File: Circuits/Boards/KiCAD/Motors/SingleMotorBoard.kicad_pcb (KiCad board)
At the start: 2 copper layers, 63.5 x 84.8 mm, 45 parts, among them M1 IRFS7537PBF, M2 IRFS7537PBF, M3 IRFS7537PBF, M4 IRFS7537PBF, Q1 2N3904, Q2 2N3904, Q3 2N3904, Q4 2N3904, Q5 2N3904, Q6 2N3904, Q7 2N3904, Q8 2N3904

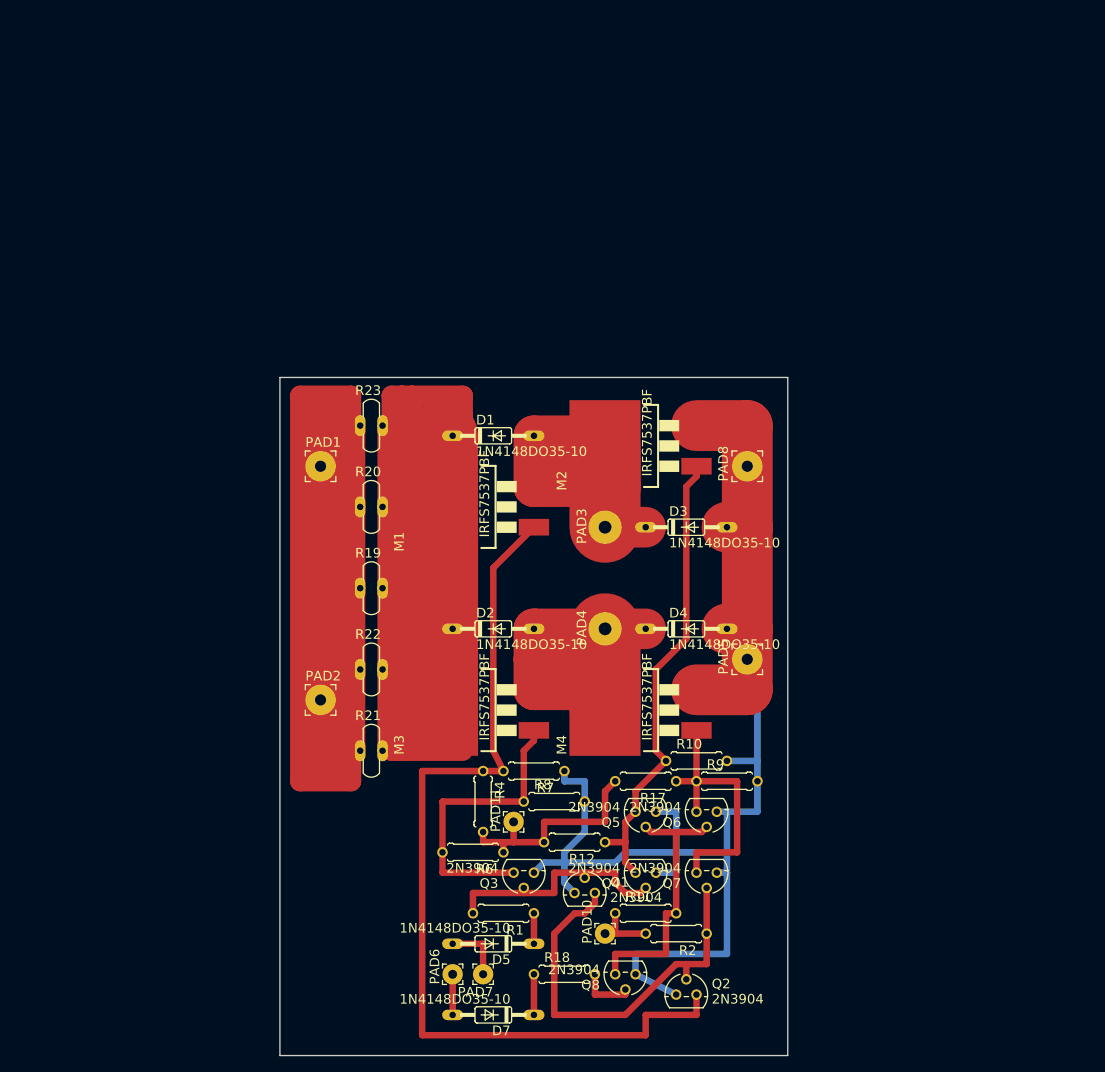
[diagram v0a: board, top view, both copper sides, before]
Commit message: Update KiCAD motor controller and Version 2 simulation
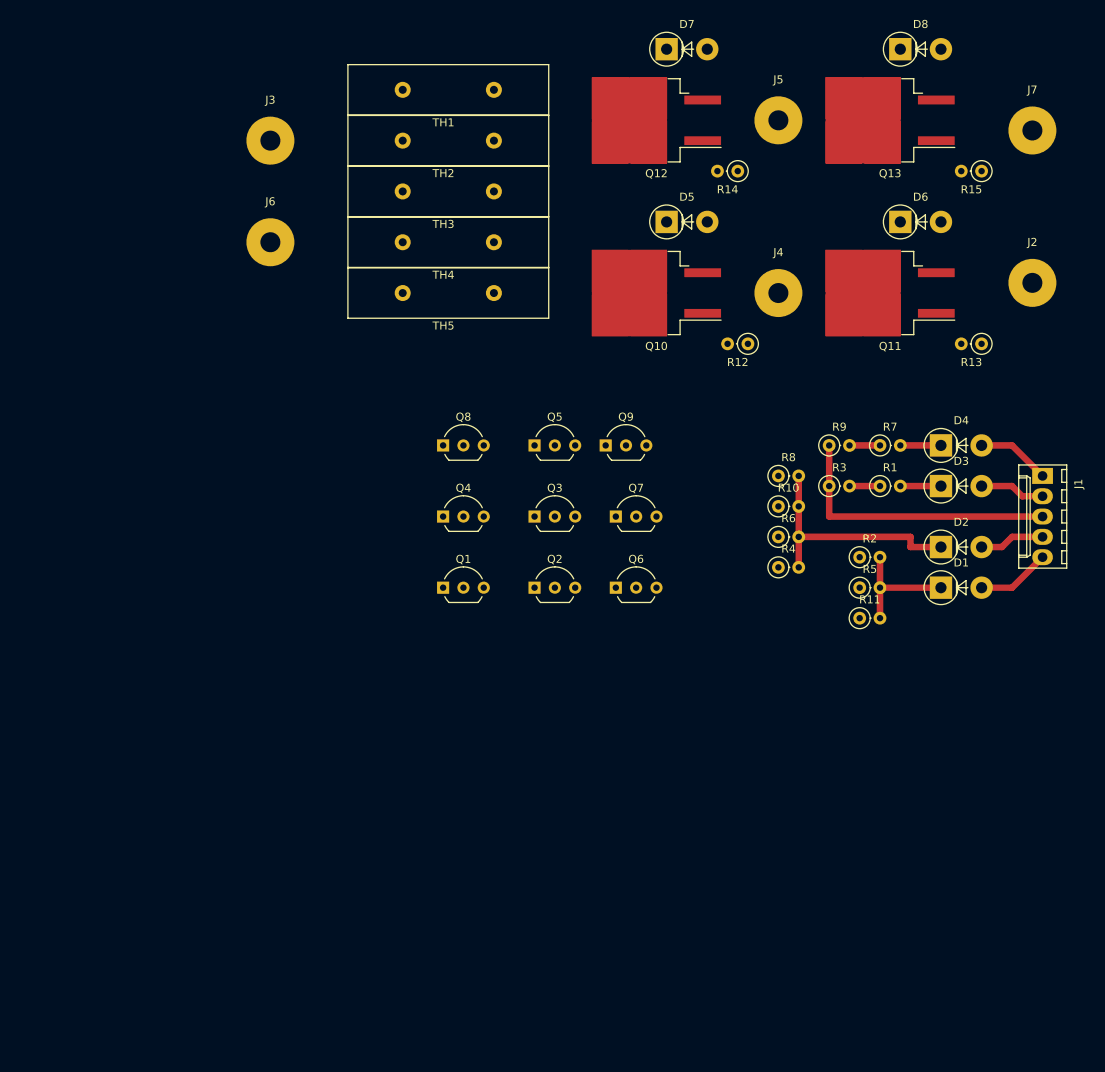
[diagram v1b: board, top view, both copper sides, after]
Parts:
- removed M1, M2, M3, M4: IRFS7537PBF, D2PACK
- removed PAD1, PAD2, PAD5, PAD8: , 3,81%2f1,4
- removed PAD10, PAD11, PAD6: , 2,54%2f1,1
- removed PAD3, PAD4: WIREPAD4,16O1,6, 4,16O1,6
- removed PAD7: , 2,54%2f1,0
- removed R17, R18: , 0207%2f7
- removed R19, R20, R21, R22, R23: , P660A
- added D6: 1N4007, Diodes_THT:D_5W_P5.08mm_Vertical_AnodeUp, F.Cu at (194.3, 43.2)
- added D8: 1N4007, Diodes_THT:D_5W_P5.08mm_Vertical_AnodeUp, F.Cu at (194.3, 21.6)
- added J1: Conn_01x05, Connectors_Molex:Molex_KK-6410-05_05x2.54mm_Straight, F.Cu at (212.1, 74.9)
- added J2: Conn_01x01, Wire_Pads:SolderWirePad_single_2-5mmDrill, F.Cu at (210.8, 50.8)
- added J3: Conn_01x01, Wire_Pads:SolderWirePad_single_2-5mmDrill, F.Cu at (115.6, 33.0)
- added J4: Conn_01x01, Wire_Pads:SolderWirePad_single_2-5mmDrill, F.Cu at (179.1, 52.1)
- added J5: Conn_01x01, Wire_Pads:SolderWirePad_single_2-5mmDrill, F.Cu at (179.1, 30.5)
- added J6: Conn_01x01, Wire_Pads:SolderWirePad_single_2-5mmDrill, F.Cu at (115.6, 45.7)
- added J7: Conn_01x01, Wire_Pads:SolderWirePad_single_2-5mmDrill, F.Cu at (210.8, 31.8)
- added Q10: Q_NMOS_DGS, TO_SOT_Packages_SMD:TO-263-2, F.Cu at (163.8, 52.1)
- added Q11: Q_NMOS_DGS, TO_SOT_Packages_SMD:TO-263-2, F.Cu at (193.0, 52.1)
- added Q12: Q_NMOS_DGS, TO_SOT_Packages_SMD:TO-263-2, F.Cu at (163.8, 30.5)
- added Q13: Q_NMOS_DGS, TO_SOT_Packages_SMD:TO-263-2, F.Cu at (193.0, 30.5)
- added Q9: 2N3904, TO_SOT_Packages_THT:TO-92_Inline_Wide, F.Cu at (157.5, 71.1)
- added R13: 10K, Resistors_THT:R_Axial_DIN0207_L6.3mm_D2.5mm_P2.54mm_Vertical, F.Cu at (204.5, 58.4)
- added R14: 1Meg, Resistors_THT:R_Axial_DIN0207_L6.3mm_D2.5mm_P2.54mm_Vertical, F.Cu at (174.0, 36.8)
- added R15: 10K, Resistors_THT:R_Axial_DIN0207_L6.3mm_D2.5mm_P2.54mm_Vertical, F.Cu at (204.5, 36.8)
- added R3: 10K, Resistors_THT:R_Axial_DIN0207_L6.3mm_D2.5mm_P2.54mm_Vertical, F.Cu at (185.4, 76.2)
- added R5: 1K, Resistors_THT:R_Axial_DIN0207_L6.3mm_D2.5mm_P2.54mm_Vertical, F.Cu at (189.2, 88.9)
- added TH1: Thermistor_PTC, Fuse_Holders_and_Fuses:Fuse_Littelfuse-LVR200, F.Cu at (143.5, 26.7)
- added TH2: Thermistor_PTC, Fuse_Holders_and_Fuses:Fuse_Littelfuse-LVR200, F.Cu at (143.5, 33.0)
- added TH3: Thermistor_PTC, Fuse_Holders_and_Fuses:Fuse_Littelfuse-LVR200, F.Cu at (143.5, 39.4)
- added TH4: Thermistor_PTC, Fuse_Holders_and_Fuses:Fuse_Littelfuse-LVR200, F.Cu at (143.5, 45.7)
- added TH5: Thermistor_PTC, Fuse_Holders_and_Fuses:Fuse_Littelfuse-LVR200, F.Cu at (143.5, 52.1)
- D1, D2, D3, D4, D5, D7: value 1N4148DO35-10 -> 1N4007; footprint DO35-10 -> Diodes_THT:D_5W_P5.08mm_Vertical_AnodeUp
- Q1, Q2, Q3, Q4, Q5, Q6, Q7, Q8: footprint TO92 -> TO_SOT_Packages_THT:TO-92_Inline_Wide
- R1, R10, R4, R6, R7, R8, R9: value (none) -> 10K; footprint 0207%2f7 -> Resistors_THT:R_Axial_DIN0207_L6.3mm_D2.5mm_P2.54mm_Vertical
- R11, R2: value (none) -> 1K; footprint 0207%2f7 -> Resistors_THT:R_Axial_DIN0207_L6.3mm_D2.5mm_P2.54mm_Vertical
- R12: value (none) -> 1Meg; footprint 0207%2f7 -> Resistors_THT:R_Axial_DIN0207_L6.3mm_D2.5mm_P2.54mm_Vertical
- moved D7 122.6 mm to (165.1, 21.6), turned to 0 degrees
- moved D5 92.8 mm to (165.1, 43.2), turned to 0 degrees
- moved R1 71.2 mm to (191.8, 76.2), turned to 0 degrees
- moved Q8 69.9 mm to (137.2, 71.1), turned to 0 degrees
- moved R12 66.0 mm to (175.3, 58.4)
- moved R7 59.4 mm to (191.8, 71.1), turned to 0 degrees
- moved D1 59.1 mm to (199.4, 88.9)
- moved D2 56.9 mm to (199.4, 83.8)
- moved R6 54.9 mm to (179.1, 82.5), turned to 0 degrees
- moved Q2 54.3 mm to (148.6, 88.9)
- moved R2 52.3 mm to (189.2, 85.1), turned to 0 degrees
- moved Q4 51.2 mm to (137.2, 80.0), turned to 0 degrees
- moved R8 49.4 mm to (179.1, 74.9)
- moved Q5 47.8 mm to (148.6, 71.1), turned to 0 degrees
- moved R4 47.1 mm to (179.1, 86.4), turned to 0 degrees
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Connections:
- Q1 pad 1: FB -> GND
- Q1 pad 2: BB -> /MBB
- Q1 pad 3: 0 -> /BBM
- Q2 pad 1: FF -> GND
- Q2 pad 2: FB -> /MFB
- Q2 pad 3: 0 -> /MBB
- Q3 pad 1: BF -> GND
- Q3 pad 2: BB -> Net-(Q3-Pad2)
- Q3 pad 3: 0 -> /MFB
- Q4 pad 1: N$20 -> GND
- Q4 pad 2: BB -> /iSpeed
- Q4 pad 3: 0 -> /BBM
- Q5 pad 1: N$20 -> GND
- Q5 pad 2: N$16 -> /MFB
- Q5 pad 3: 0 -> /MFF
- Q6 pad 1: N$27 -> GND
- Q6 pad 2: N$16 -> /MFB
- Q6 pad 3: 0 -> /FBM
- Q7 pad 1: N$27 -> GND
- Q7 pad 2: FB -> /MBB
- Q7 pad 3: 0 -> /MBF
- Q8 pad 1: N$16 -> GND
- Q8 pad 2: N$23 -> Net-(Q8-Pad2)
- Q8 pad 3: 0 -> /iSpeed
- R1 pad 1: N$19 -> Net-(Q3-Pad2)
- R1 pad 2: BB -> /Dir
- R10 pad 1: N$20 -> /MBF
- R10 pad 2: 0 -> /VG
- R11 pad 1: VSW -> /iSpeed
- R11 pad 2: N$16 -> /VSW
- R12 pad 1: N$20 -> GND
- R12 pad 2: VG -> /MFF
- R2 pad 1: FB -> /MBB
- R2 pad 2: VSW -> /VSW
- R4 pad 1: FF -> /BBM
- R4 pad 2: VG -> /VG
- R6 pad 1: VG -> /MFF
- R6 pad 2: BF -> /VG
- R7 pad 1: 0 -> Net-(Q8-Pad2)
- R7 pad 2: FF -> /Speed
- R8 pad 1: BF -> /FBM
- R8 pad 2: 0 -> /VG
- R9 pad 1: N$27 -> GND
- R9 pad 2: 0 -> Net-(Q8-Pad2)
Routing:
- net VDD: track 255.7 -> 0.00 mm
- net VBAT: track 221.8 -> 0.00 mm
- net 0: track 184.8 -> 0.00 mm
- net FF: track 115.4 -> 0.00 mm
- net MP: track 59.3 -> 0.00 mm
- net N$20: track 58.6 -> 0.00 mm
- net MN: track 53.6 -> 0.00 mm
- net FB: track 51.2 -> 0.00 mm
- net BF: track 37.4 -> 0.00 mm
- net GND: track 0.00 -> 35.6 mm
- net N$27: track 34.3 -> 0.00 mm
- net N$16: track 33.5 -> 0.00 mm
- net /VG: track 0.00 -> 30.5 mm
- net BB: track 30.0 -> 0.00 mm
- net VG: track 28.5 -> 0.00 mm
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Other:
- board outline removed
- net class Default: clearance 0.1524 -> 0.254; trace_width 0.25 -> 0.8128; via_dia 0.6 -> 0.889; via_drill 0.4 -> 0.8128
- rule pad_to_mask_clearance: 0.2 -> 0
- rule trace_clearance: 0.1524 -> 0.254
- rule trace_min: 0.1524 -> 0.254
- rule via_min_drill: 0.3 -> 0.8128
- rule via_min_size: 0.4 -> 0.889

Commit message: Fixed KiCAD motor controller
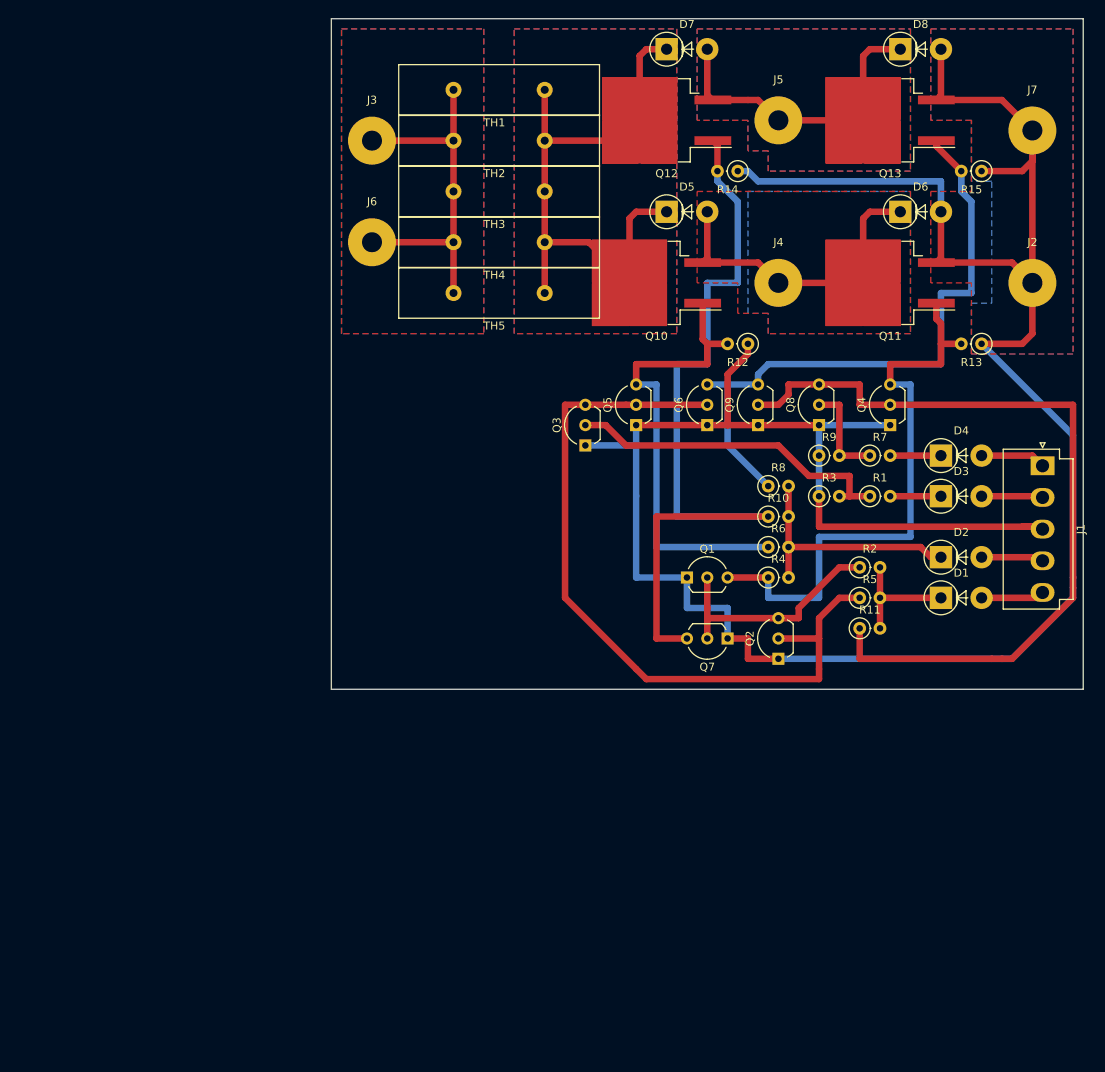
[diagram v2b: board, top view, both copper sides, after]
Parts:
- J1: footprint Connectors_Molex:Molex_KK-6410-05_05x2.54mm_Straight -> Connectors_JST:JST_VH_B5P-VH-B_5x3.96mm_Vertical
- moved Q4 57.0 mm to (193.0, 68.6), turned to 90 degrees
- moved Q8 47.1 mm to (184.2, 68.6), turned to 90 degrees
- moved Q2 31.7 mm to (179.1, 97.8), turned to 90 degrees
- moved Q1 30.5 mm to (167.6, 87.6)
- moved Q6 23.3 mm to (170.2, 68.6), turned to 90 degrees
- moved Q7 20.7 mm to (172.7, 95.2), turned to 180 degrees
- moved Q9 19.2 mm to (176.5, 68.6), turned to 90 degrees
- moved Q5 13.0 mm to (161.3, 68.6), turned to 90 degrees
- moved J3 12.7 mm to (128.3, 33.0)
- moved J6 12.7 mm to (128.3, 45.7)
- moved Q3 10.9 mm to (154.9, 71.1), turned to 90 degrees
- moved TH1 6.35 mm to (149.9, 26.7)
- moved TH2 6.35 mm to (149.9, 33.0)
- moved TH3 6.35 mm to (149.9, 39.4)
- moved TH4 6.35 mm to (149.9, 45.7)
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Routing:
- net GND: track 35.6 -> 330.4 mm
- net /iSpeed: track 0.00 -> 101.5 mm
- net /MBF: track 0.00 -> 100.4 mm
- net /MFB: track 0.00 -> 96.7 mm
- net /FBM: track 0.00 -> 79.4 mm
- net Net-(D5-Pad1): track 0.00 -> 75.8 mm
- net /BBM: track 0.00 -> 73.9 mm
- net /MFF: track 0.00 -> 58.7 mm
- net Net-(J3-Pad1): track 0.00 -> 45.8 mm
- net Net-(D5-Pad2): track 0.00 -> 40.7 mm
- net Net-(D7-Pad2): track 0.00 -> 39.6 mm
- net Net-(Q3-Pad2): track 3.81 -> 42.0 mm
- net /MBB: track 0.00 -> 30.0 mm
- net Net-(Q8-Pad2): track 3.81 -> 12.7 mm
- net /Speed: track 5.08 -> 6.35 mm
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- added copper zone on B.Cu, net GND
- added copper zone on F.Cu, net GND
- added copper zone on B.Cu, net Net-(D5-Pad1)
- added copper zone on F.Cu, net Net-(D5-Pad1)
- added copper zone on B.Cu, net Net-(D5-Pad2)
- added copper zone on F.Cu, net Net-(D5-Pad2)
- added copper zone on B.Cu, net Net-(D7-Pad2)
- added copper zone on F.Cu, net Net-(D7-Pad2)
- added copper zone on B.Cu, net Net-(J3-Pad1)
- added copper zone on F.Cu, net Net-(J3-Pad1)
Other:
- board outline added: 94 x 83.8 mm

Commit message: Rerouted motor controller for smaller size
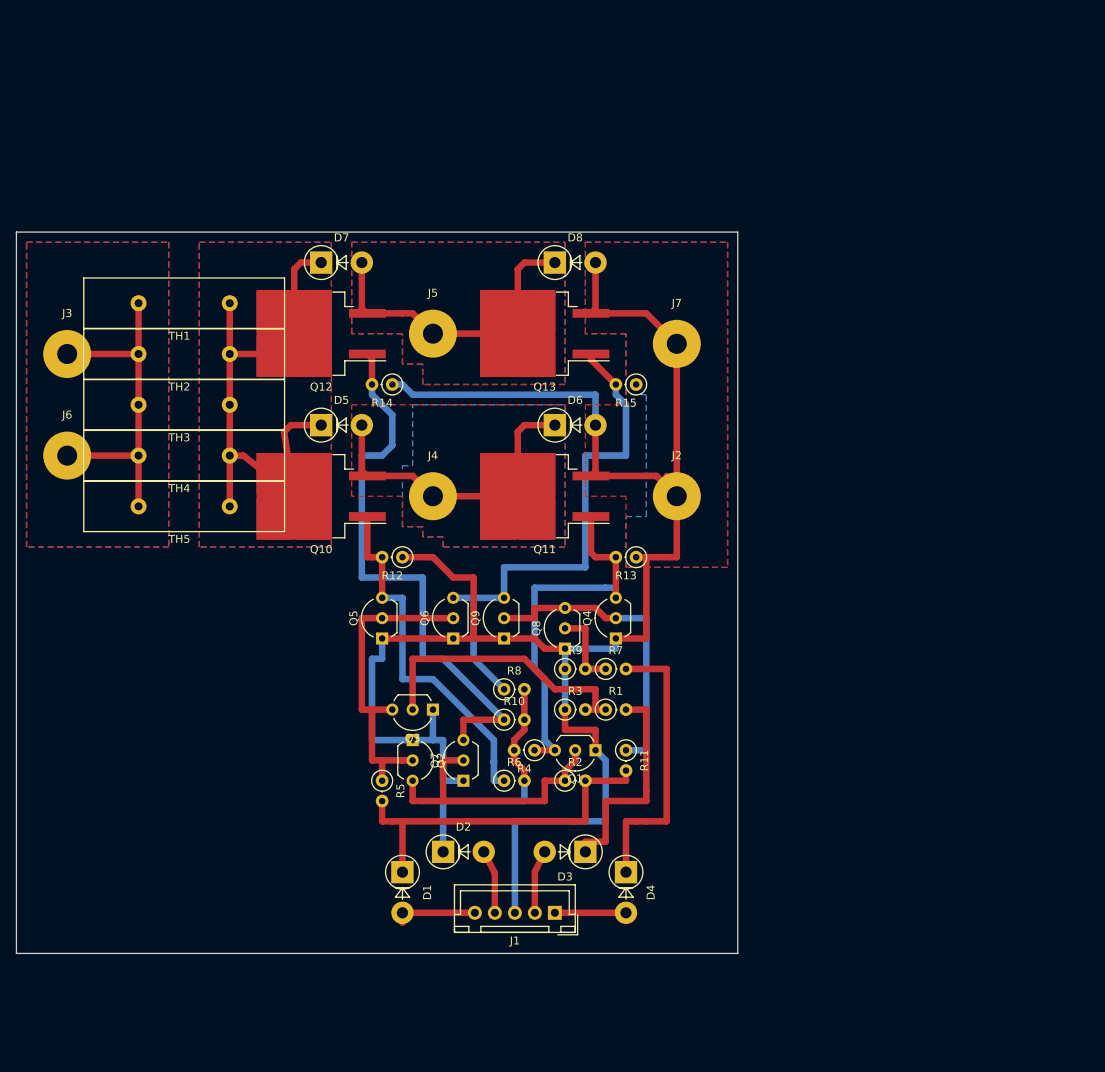
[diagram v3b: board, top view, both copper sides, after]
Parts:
- J1: footprint Connectors_JST:JST_VH_B5P-VH-B_5x3.96mm_Vertical -> Connectors_JST:JST_XH_B05B-XH-A_05x2.50mm_Straight
- moved J1 82.7 mm to (151.1, 129.5), turned to 180 degrees
- moved D1 75.5 mm to (132.1, 124.5), turned to 270 degrees
- moved D2 72.3 mm to (137.2, 121.9)
- moved D4 65.3 mm to (160.0, 124.5), turned to 270 degrees
- moved R5 63.9 mm to (129.5, 113.0), turned to 270 degrees
- moved D3 62.9 mm to (154.9, 121.9), turned to 180 degrees
- moved J2 51.8 mm to (166.4, 77.5)
- moved J7 51.8 mm to (166.4, 58.4)
- moved D6 50.8 mm to (151.1, 68.6)
- moved D8 50.8 mm to (151.1, 48.3)
- moved J4 50.8 mm to (135.9, 77.5)
- moved J5 50.8 mm to (135.9, 57.1)
- moved R13 50.8 mm to (161.3, 85.1)
- moved R14 50.8 mm to (130.8, 63.5)
- moved R15 50.8 mm to (161.3, 63.5)
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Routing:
- net GND: track 330.4 -> 250.3 mm
- net /iSpeed: track 101.5 -> 38.6 mm
- net /MFB: track 96.7 -> 40.6 mm
- net /VSW: track 15.2 -> 45.7 mm
- net /MBF: track 100.4 -> 71.0 mm
- net /Speed: track 6.35 -> 35.6 mm
- net /BBM: track 73.9 -> 48.3 mm
- net /Dir: track 6.35 -> 27.9 mm
- net /FBM: track 79.4 -> 66.9 mm
- net /MFF: track 58.7 -> 46.3 mm
- net Net-(D5-Pad1): track 75.8 -> 69.3 mm
- net Net-(Q3-Pad2): track 42.0 -> 35.9 mm
- net /MBB: track 30.0 -> 36.1 mm
- net Net-(Q8-Pad2): track 12.7 -> 10.2 mm
- net Net-(J3-Pad1): track 45.8 -> 43.2 mm
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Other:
- board size 94 x 83.8 mm -> 90.2 x 90.2 mm

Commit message: Adjusted PCB design
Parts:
- moved R14 1.27 mm to (132.1, 63.5)
- moved Q11 1.27 mm to (151.1, 77.5)
- moved Q13 1.27 mm to (151.1, 57.1)
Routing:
- net GND: track 250.3 -> 248.2 mm
- net /BBM: track 48.3 -> 46.3 mm
- net Net-(D5-Pad2): track 39.6 -> 40.9 mm
- net Net-(D7-Pad2): track 39.6 -> 40.9 mm
- net /FBM: track 66.9 -> 66.4 mm
